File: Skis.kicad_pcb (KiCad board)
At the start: 2 copper layers, 29.2 x 109.2 mm, 96 parts, among them J1 TRIG_A, J10 SIGNAL_OUT_B, J11 ENV_OUT_B, J2 CV_IN_A, J3 SIGNAL_IN_A, J4 SIGNAL_OUT_A, J5 ENV_OUT_A, J6 EuroPower, J7 TRIG_B, J8 CV_IN_B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

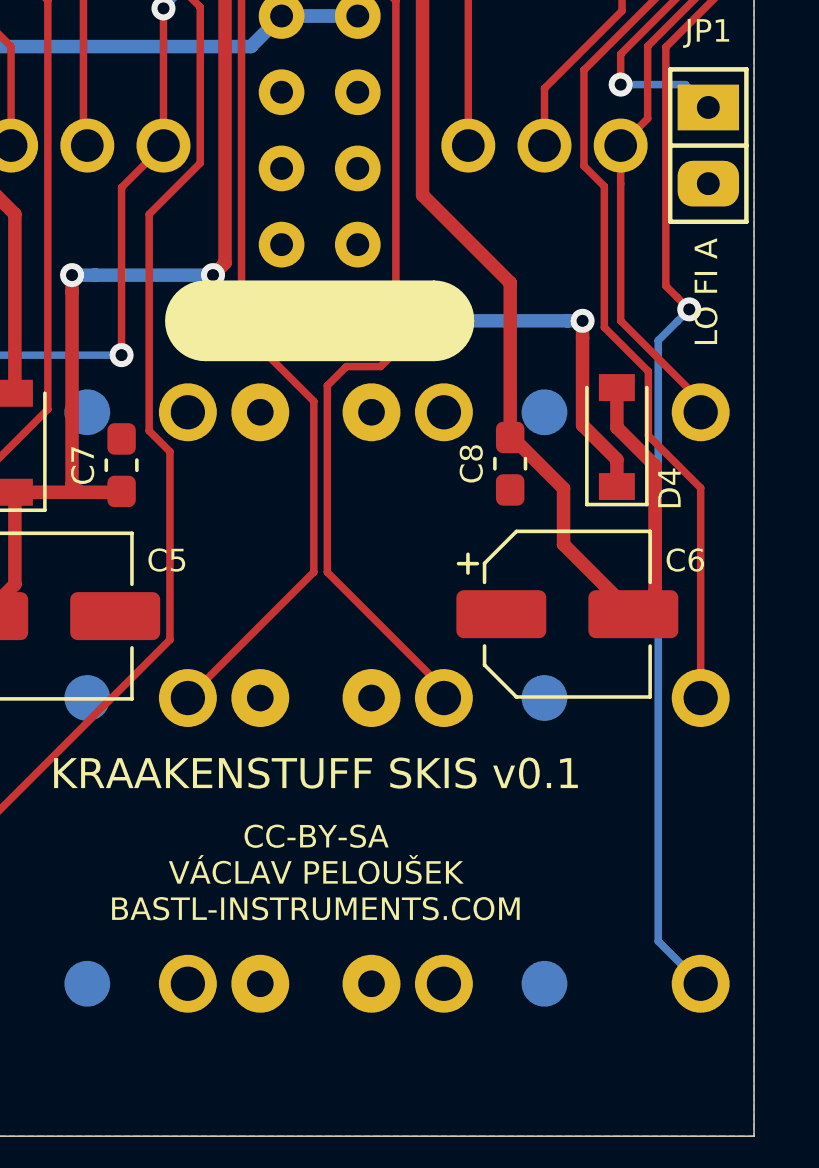
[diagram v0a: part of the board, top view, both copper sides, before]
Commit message: Added normalization for input jacks
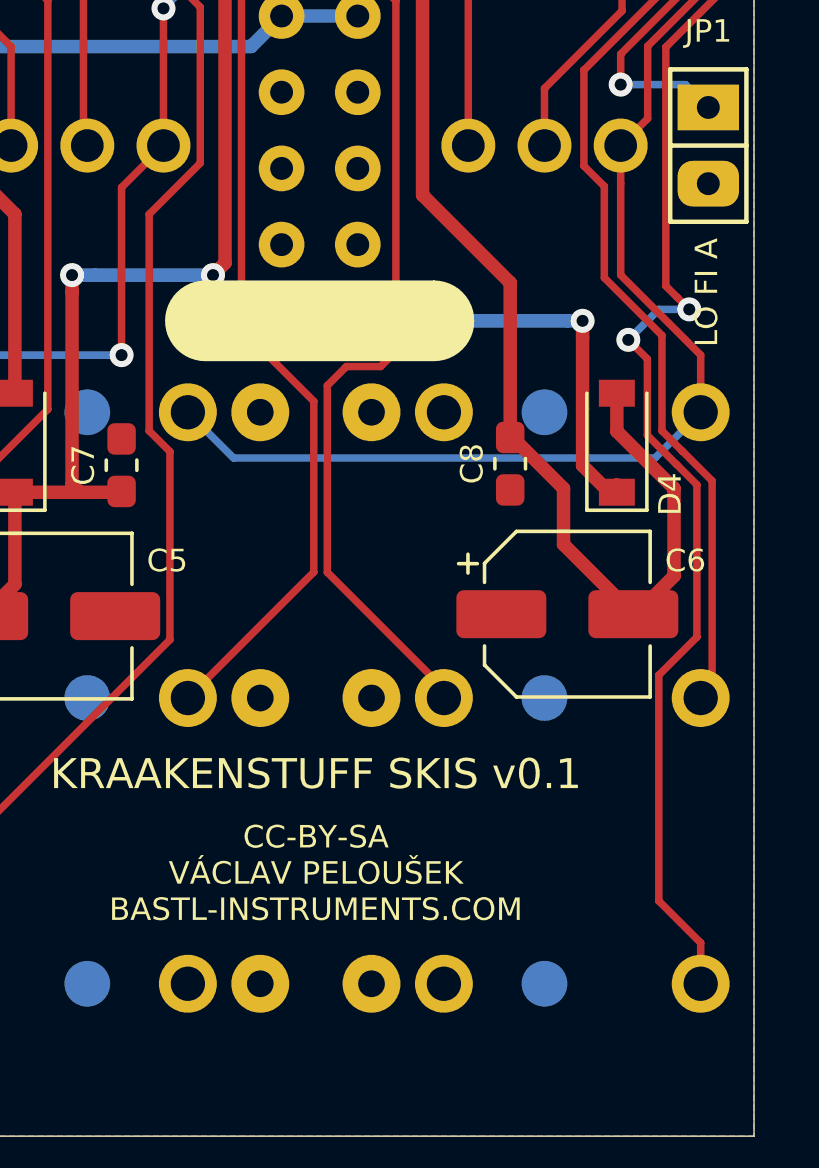
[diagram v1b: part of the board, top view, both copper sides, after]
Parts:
- moved D4 0.19 mm to (94.5, 103.9)
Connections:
- J3 pad T: Net-(J3-PadT) -> NORM_IN
- J9 pad TN: GND -> NORM_IN
- Q1 pad 3: Net-(J3-PadT) -> NORM_IN
- SW1 pad 1: Net-(J3-PadT) -> NORM_IN
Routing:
- net NORM_IN: track 0.00 -> 50.7 mm
- net Net-(J3-PadT): track 32.4 -> 0.00 mm
- net Net-(J4-PadT): track 57.2 -> 59.6 mm, vias 1 -> 2

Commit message: Changed version number on pcb
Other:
- board text added: "KRAAKENSTUFF SKIS v0.2"
- board text removed: "KRAAKENSTUFF SKIS v0.1"
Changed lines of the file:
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@@
     (effects (font (size 0.75 0.75) (thickness 0.12)))
   )
-  (gr_text "KRAAKENSTUFF SKIS v0.1" (at 84.455 114.935) (layer F.SilkS)
+  (gr_text "KRAAKENSTUFF SKIS v0.2" (at 84.455 114.935) (layer F.SilkS)
     (effects (font (size 1 1) (thickness 0.15)))
   )
